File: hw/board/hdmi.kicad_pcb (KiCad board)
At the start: 2 copper layers, 41.7 x 34.3 mm, 7 parts, among them J1 HDMI_A, J2 HDMI_A, J3 Connector

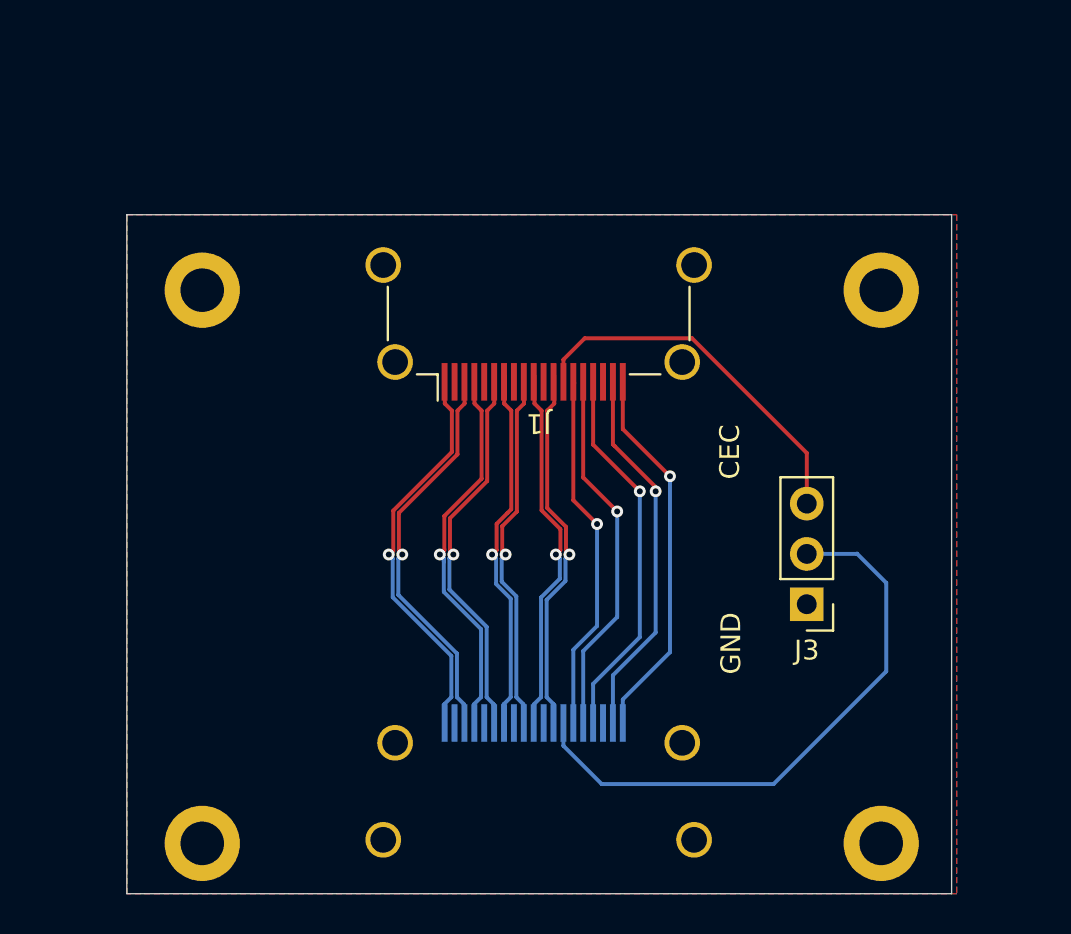
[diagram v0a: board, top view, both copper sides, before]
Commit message: PCB with pullup resistors
Added 3.3v pin from Rpi to board, 27K Ohm pullup resistors, and diodes to conform to CEC spec.
Add cec-gpio configuration script.
Add HW specific readme.
Design is still just a guess.
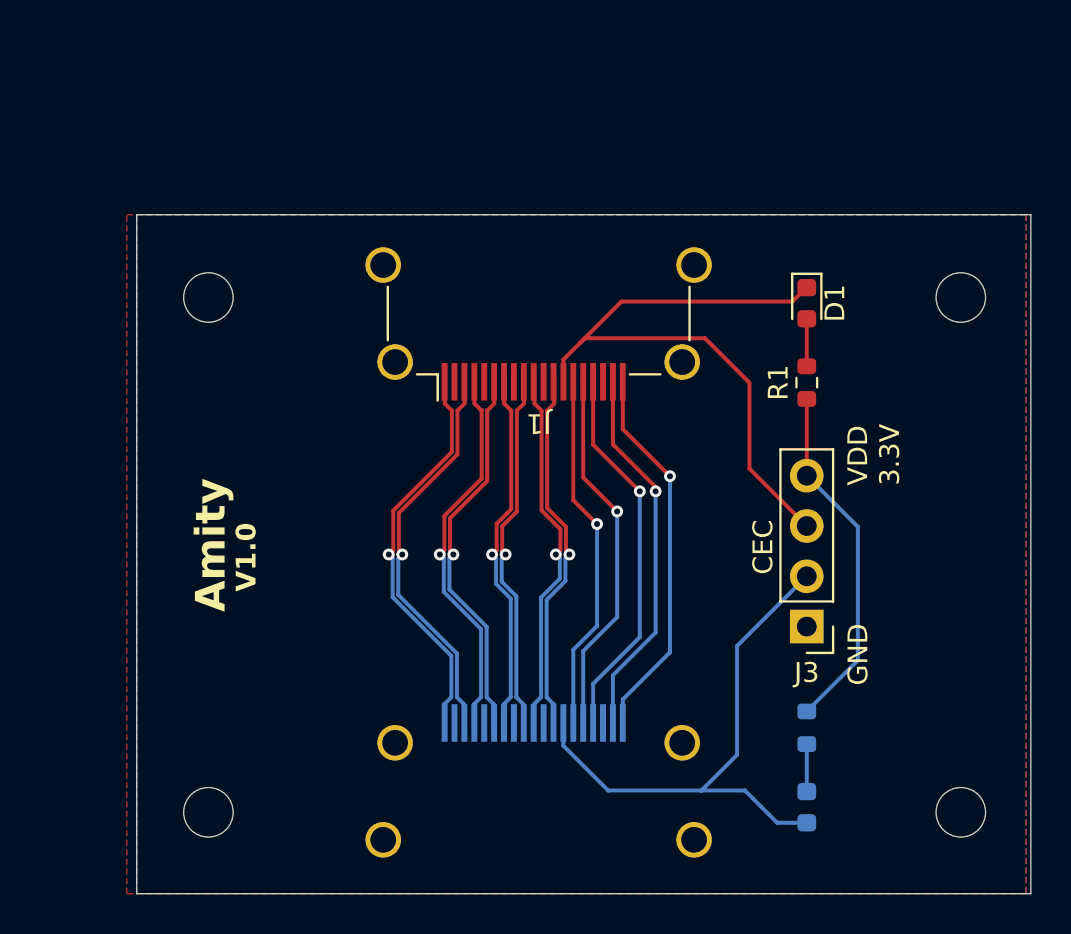
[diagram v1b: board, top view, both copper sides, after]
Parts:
- removed REF** (x4): MountingHole_2.2mm_M2_DIN965_Pad, MountingHole:MountingHole_2.2mm_M2_DIN965_Pad
- added D1: 4148, Diode_SMD:D_0603_1608Metric, F.Cu at (153.7, 88.3)
- added D2: 4148, Diode_SMD:D_0603_1608Metric, B.Cu at (153.7, 113.7)
- added H1: MountingHole, MountingHole:MountingHole_2.5mm, F.Cu at (123.5, 88.0)
- added H2: MountingHole, MountingHole:MountingHole_2.5mm, F.Cu at (123.5, 114.0)
- added H3: MountingHole, MountingHole:MountingHole_2.5mm, F.Cu at (161.5, 88.0)
- added H4: MountingHole, MountingHole:MountingHole_2.5mm, F.Cu at (161.5, 114.0)
- added R1: 27K, Resistor_SMD:R_0603_1608Metric, F.Cu at (153.7, 92.3)
- added R2: 27K, Resistor_SMD:R_0603_1608Metric, B.Cu at (153.7, 109.7)
- J3: value Connector -> Conn_01x04_Pin; footprint Connector_PinHeader_2.54mm:PinHeader_1x03_P2.54mm_Vertical -> Connector_PinHeader_2.54mm:PinHeader_1x04_P2.54mm_Vertical
- moved J3 1.13 mm to (153.7, 104.6)
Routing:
- net VDD: track 0.00 -> 17.9 mm
- net Net-(D1-K): track 18.8 -> 32.9 mm
- net Net-(D1-A): track 0.00 -> 2.48 mm
- net Net-(D2-A): track 0.00 -> 2.40 mm
- net Net-(D2-K): track 29.7 -> 28.1 mm
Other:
- board size 41.7 x 34.3 mm -> 45.2 x 34.3 mm
- board text added: "Amity"
- board text added: "V1.0"
- board text added: "VDD 3.3V"

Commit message: PCB v2
4 Layers. More regular board dimensions. Thicker, straighter, shorter, better separated, equal length,
high speed traces.

No DRC violations.
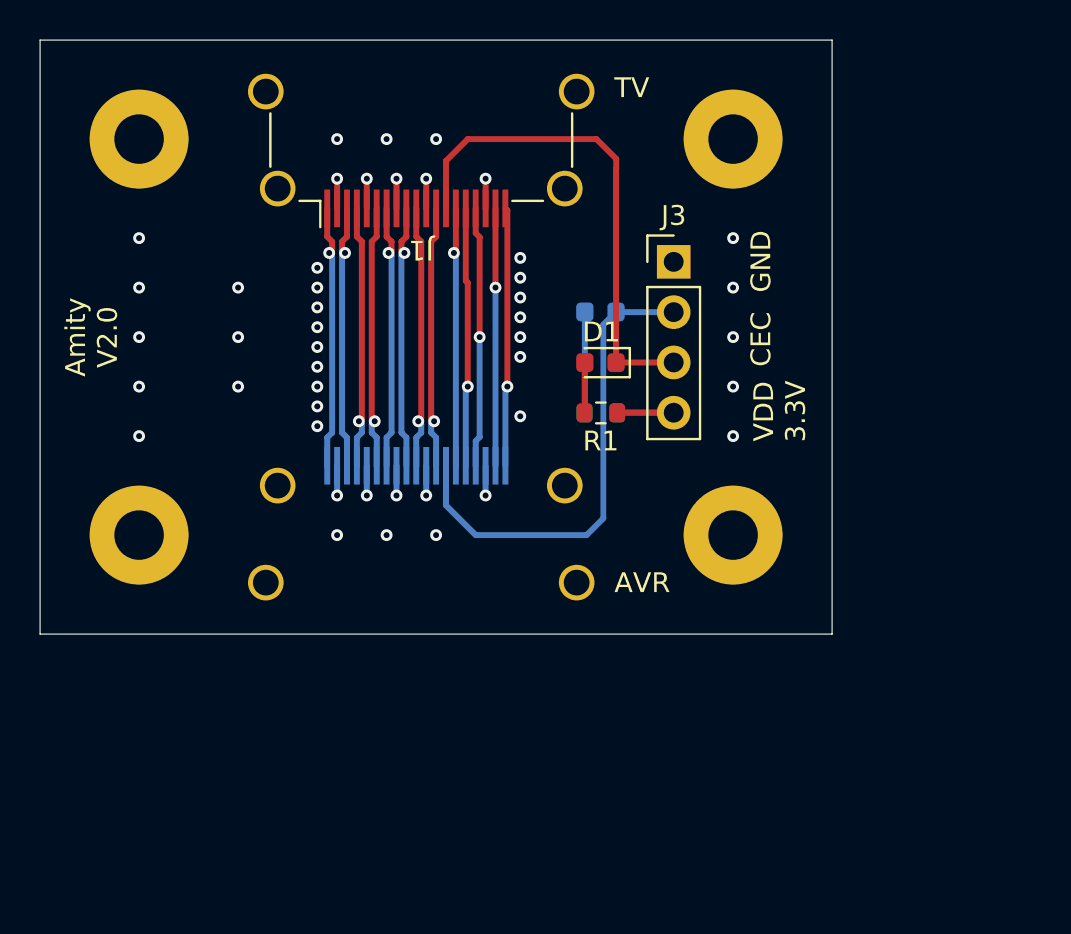
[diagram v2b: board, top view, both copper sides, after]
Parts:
- H1, H2, H3, H4: value MountingHole -> ~; footprint MountingHole:MountingHole_2.5mm -> MountingHole:MountingHole_2.5mm_Pad
- moved H3 43.2 mm to (120.0, 100.0)
- moved H2 43.1 mm to (150.0, 80.0)
- moved D2 27.1 mm to (143.3, 88.7), turned to 180 degrees
- moved J3 19.6 mm to (147.0, 86.2), turned to 0 degrees
- moved R2 19.0 mm to (143.3, 93.8), turned to 180 degrees
- moved H4 18.1 mm to (150.0, 100.0)
- moved J2 14.3 mm to (134.2, 101.5)
- moved D1 10.8 mm to (143.3, 91.3), turned to 180 degrees
- moved J1 10.6 mm to (134.2, 78.5)
- moved R1 10.5 mm to (143.3, 93.8), turned to 180 degrees
- moved H1 8.73 mm to (120.0, 80.0)
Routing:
- net GND: track 0.00 -> 15.0 mm, vias 0 -> 45
- net VDD: track 17.9 -> 5.73 mm
- net Net-(D1-K): track 32.9 -> 25.1 mm
- net /D2+: track 21.0 -> 13.3 mm
- net /D2-: track 21.0 -> 13.3 mm
- net /D1+: track 20.2 -> 13.3 mm
- net /D1-: track 20.1 -> 13.3 mm
- net Net-(J1-HPD): track 19.2 -> 13.1 mm
- net Net-(J1-+5V): track 19.0 -> 13.0 mm
- net Net-(J1-SDA): track 19.2 -> 13.2 mm
- net /CK+: track 19.3 -> 13.3 mm
- net /CK-: track 19.3 -> 13.3 mm
- net /D0+: track 19.1 -> 13.3 mm
- net /D0-: track 19.0 -> 13.3 mm
- net Net-(J1-SCL): track 18.7 -> 13.1 mm
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- added copper zone on In1.Cu, net GND
- added copper zone on In2.Cu, net GND
- removed copper zone on B.Cu, net GND
- removed copper zone on F.Cu, net GND
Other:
- board size 45.2 x 34.3 mm -> 40 x 30 mm
- copper layers 2 -> 4
- board text added: "AVR"
- board text added: "Amity V2.0"
- board text added: "TV"
- board text removed: "Amity"
- board text removed: "V1.0"
